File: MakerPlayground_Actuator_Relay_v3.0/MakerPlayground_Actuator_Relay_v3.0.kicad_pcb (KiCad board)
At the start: 2 copper layers, 45.5 x 19.9 mm, 8 parts, among them J1 Conn_01x04, J2 Terminal Block, J3 Terminal Block, K1 SANYOU_SRD_Form_C, Q1 Q_NPN_BEC

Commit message: Under editing mounting hole.
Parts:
- added REF**: MountingHole_3mm, MountingHole:MountingHole_3mm, F.Cu at (128.5, 112.5)
- added REF**: MountingHole_3mm, MountingHole:MountingHole_3mm, F.Cu at (128.5, 87.5)
- added REF**: MountingHole_3mm, MountingHole:MountingHole_3mm, F.Cu at (158.5, 112.5)
- added REF**: MountingHole_3mm, MountingHole:MountingHole_3mm, F.Cu at (158.5, 87.5)
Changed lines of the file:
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@@
-(kicad_pcb (version 20171130) (host pcbnew "(5.0.0-rc2-178-g3c7b91b96)")
+(kicad_pcb (version 20171130) (host pcbnew 5.0.2-5.fc29)
   (general
     (thickness 1.6)
-    (drawings 308)
+    (drawings 313)
     (tracks 21)
     (zones 0)
-    (modules 8)
+    (modules 12)
     (nets 9)
   )
   (page A4)
   (layers
-    (0 F.Cu signal)
-    (31 B.Cu signal)
+    (0 F.Cu signal hide)
+    (31 B.Cu signal hide)
     (32 B.Adhes user)
     (33 F.Adhes user)
@@
     (46 B.CrtYd user)
     (47 F.CrtYd user)
-    (48 B.Fab user)
-    (49 F.Fab user)
+    (48 B.Fab user hide)
+    (49 F.Fab user hide)
   )
   (setup
@@
     (pad_drill 0.762)
     (pad_to_mask_clearance 0.2)
+    (solder_mask_min_width 0.25)
     (aux_axis_origin 0 0)
     (visible_elements 7FFFFFFF)
@@
       (drillshape 0)
       (scaleselection 1)
-      (outputdirectory gerber/))
+      (outputdirectory "gerber/"))
   )
   (net 0 "")
@@
     (add_net SIG)
     (add_net VCC)
+  )
+  (module MountingHole:MountingHole_3mm (layer F.Cu)
+    (at 128.5 112.5 180)
+    (descr "Mounting Hole 3mm, no annular")
+    (tags "mounting hole 3mm no annular")
+    (attr virtual)
+    (fp_text reference REF** (at 0 -4 180) (layer F.SilkS) hide
+      (effects (font (size 1 1) (thickness 0.15)))
+    )
+    (fp_text value MountingHole_3mm (at 0 4 180) (layer F.Fab)
+      (effects (font (size 1 1) (thickness 0.15)))
+    )
+    (fp_circle (center 0 0) (end 3.25 0) (layer F.CrtYd) (width 0.05))
+    (fp_circle (center 0 0) (end 3 0) (layer Cmts.User) (width 0.15))
+    (fp_text user %R (at 0.3 0 180) (layer F.Fab)
+      (effects (font (size 1 1) (thickness 0.15)))
+    )
+    (pad 1 np_thru_hole circle (at 0 0 180) (size 3 3) (drill 3) (layers *.Cu *.Mask))
+  )
+  (module MountingHole:MountingHole_3mm (layer F.Cu)
+    (at 128.5 87.5 180)
+    (descr "Mounting Hole 3mm, no annular")
+    (tags "mounting hole 3mm no annular")
+    (attr virtual)
+    (fp_text reference REF** (at 0 -4 180) (layer F.SilkS) hide
+      (effects (font (size 1 1) (thickness 0.15)))
+    )
+    (fp_text value MountingHole_3mm (at 0 4 180) (layer F.Fab)
+      (effects (font (size 1 1) (thickness 0.15)))
+    )
+    (fp_text user %R (at 0.3 0 180) (layer F.Fab)
+      (effects (font (size 1 1) (thickness 0.15)))
+    )
+    (fp_circle (center 0 0) (end 3 0) (layer Cmts.User) (width 0.15))
+    (fp_circle (center 0 0) (end 3.25 0) (layer F.CrtYd) (width 0.05))
+    (pad 1 np_thru_hole circle (at 0 0 180) (size 3 3) (drill 3) (layers *.Cu *.Mask))
+  )
+  (module MountingHole:MountingHole_3mm (layer F.Cu)
+    (at 158.5 112.5)
+    (descr "Mounting Hole 3mm, no annular")
+    (tags "mounting hole 3mm no annular")
+    (attr virtual)
+    (fp_text reference REF** (at 0 -4) (layer F.SilkS) hide
+      (effects (font (size 1 1) (thickness 0.15)))
+    )
+    (fp_text value MountingHole_3mm (at 0 4) (layer F.Fab)
+      (effects (font (size 1 1) (thickness 0.15)))
+    )
+    (fp_circle (center 0 0) (end 3.25 0) (layer F.CrtYd) (width 0.05))
+    (fp_circle (center 0 0) (end 3 0) (layer Cmts.User) (width 0.15))
+    (fp_text user %R (at 0.3 0) (layer F.Fab)
+      (effects (font (size 1 1) (thickness 0.15)))
+    )
+    (pad 1 np_thru_hole circle (at 0 0) (size 3 3) (drill 3) (layers *.Cu *.Mask))
+  )
+  (module MountingHole:MountingHole_3mm (layer F.Cu)
+    (at 158.5 87.5)
+    (descr "Mounting Hole 3mm, no annular")
+    (tags "mounting hole 3mm no annular")
+    (attr virtual)
+    (fp_text reference REF** (at 0 -4) (layer F.SilkS) hide
+      (effects (font (size 1 1) (thickness 0.15)))
+    )
+    (fp_text value MountingHole_3mm (at 0 4) (layer F.Fab)
+      (effects (font (size 1 1) (thickness 0.15)))
+    )
+    (fp_text user %R (at 0.3 0) (layer F.Fab)
+      (effects (font (size 1 1) (thickness 0.15)))
+    )
+    (fp_circle (center 0 0) (end 3 0) (layer Cmts.User) (width 0.15))
+    (fp_circle (center 0 0) (end 3.25 0) (layer F.CrtYd) (width 0.05))
+    (pad 1 np_thru_hole circle (at 0 0) (size 3 3) (drill 3) (layers *.Cu *.Mask))
   )
   (module GiraffeTech-Connector:TerminalBlock_Dinkle_ED350V_1x02_P3.50mm_Horizontal (layer F.Cu)
@@
       (xy 0.199355 -0.596628) (xy 0.593328 -0.992663) (xy 0.790777 -0.991434)) (layer F.SilkS) (width 0.01))
   )
+  (dimension 25 (width 0.3) (layer Dwgs.User)
+    (gr_text "25.000 mm" (at 119.9 100 90) (layer Dwgs.User)
+      (effects (font (size 1.5 1.5) (thickness 0.3)))
+    )
+    (feature1 (pts (xy 128.5 87.5) (xy 121.413579 87.5)))
+    (feature2 (pts (xy 128.5 112.5) (xy 121.413579 112.5)))
+    (crossbar (pts (xy 122 112.5) (xy 122 87.5)))
+    (arrow1a (pts (xy 122 87.5) (xy 122.586421 88.626504)))
+    (arrow1b (pts (xy 122 87.5) (xy 121.413579 88.626504)))
+    (arrow2a (pts (xy 122 112.5) (xy 122.586421 111.373496)))
+    (arrow2b (pts (xy 122 112.5) (xy 121.413579 111.373496)))
+  )
+  (dimension 25 (width 0.3) (layer Dwgs.User)
+    (gr_text "25.000 mm" (at 167.1 100 270) (layer Dwgs.User)
+      (effects (font (size 1.5 1.5) (thickness 0.3)))
+    )
+    (feature1 (pts (xy 158.5 112.5) (xy 165.586421 112.5)))
+    (feature2 (pts (xy 158.5 87.5) (xy 165.586421 87.5)))
+    (crossbar (pts (xy 165 87.5) (xy 165 112.5)))
+    (arrow1a (pts (xy 165 112.5) (xy 164.413579 111.373496)))
+    (arrow1b (pts (xy 165 112.5) (xy 165.586421 111.373496)))
+    (arrow2a (pts (xy 165 87.5) (xy 164.413579 88.626504)))
+    (arrow2b (pts (xy 165 87.5) (xy 165.586421 88.626504)))
+  )
+  (dimension 30 (width 0.3) (layer Dwgs.User)
+    (gr_text "30.000 mm" (at 143.5 79.447319) (layer Dwgs.User)
+      (effects (font (size 1.5 1.5) (thickness 0.3)))
+    )
+    (feature1 (pts (xy 158.5 86.797319) (xy 158.5 80.960898)))
+    (feature2 (pts (xy 128.5 86.797319) (xy 128.5 80.960898)))
+    (crossbar (pts (xy 128.5 81.547319) (xy 158.5 81.547319)))
+    (arrow1a (pts (xy 158.5 81.547319) (xy 157.373496 82.13374)))
+    (arrow1b (pts (xy 158.5 81.547319) (xy 157.373496 80.960898)))
+    (arrow2a (pts (xy 128.5 81.547319) (xy 129.626504 82.13374)))
+    (arrow2b (pts (xy 128.5 81.547319) (xy 129.626504 80.960898)))
+  )
+  (gr_line (start 158.5 79) (end 158.5 114.5) (layer Dwgs.User) (width 0.2))
+  (gr_line (start 128.5 81) (end 128.5 114.25) (layer Dwgs.User) (width 0.2))
   (gr_text OUT (at 159 108.5) (layer F.SilkS)
     (effects (font (size 1.5 1.5) (thickness 0.3)))

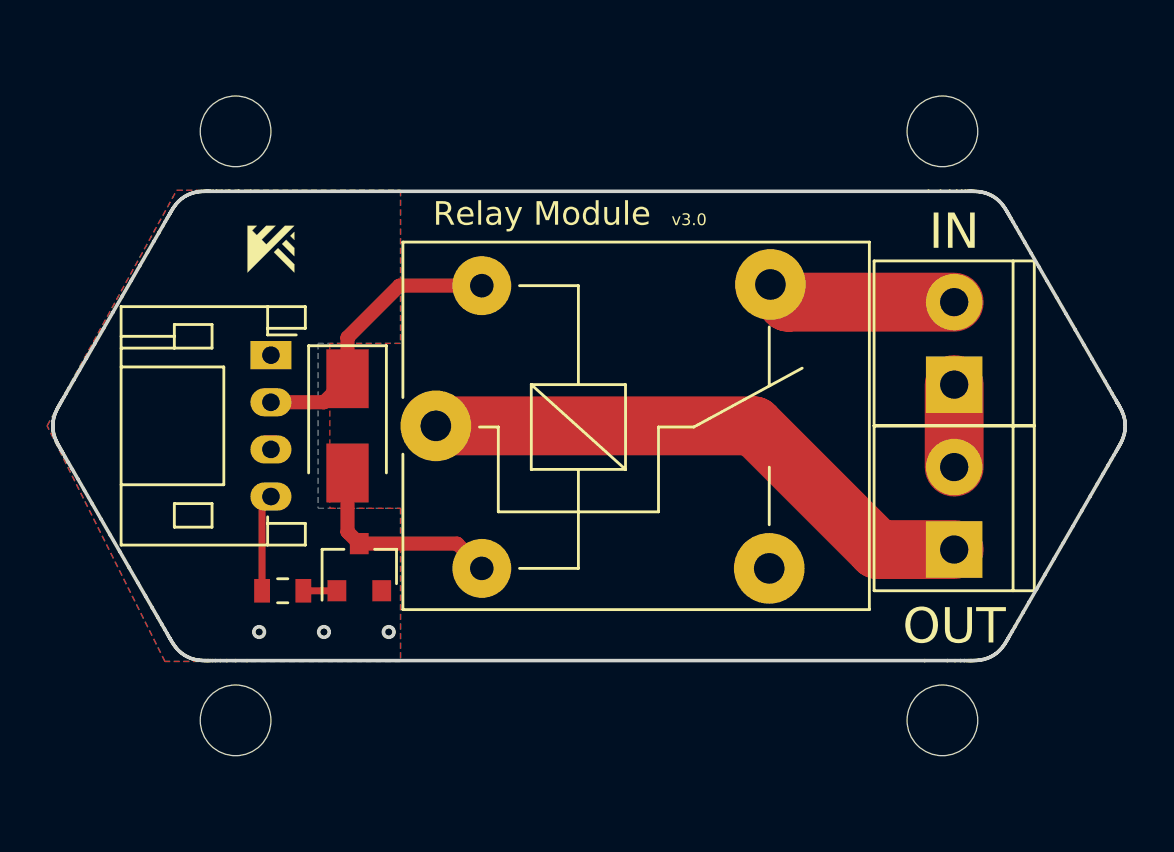
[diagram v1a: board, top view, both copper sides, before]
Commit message: Update Relay board mounting hole design.
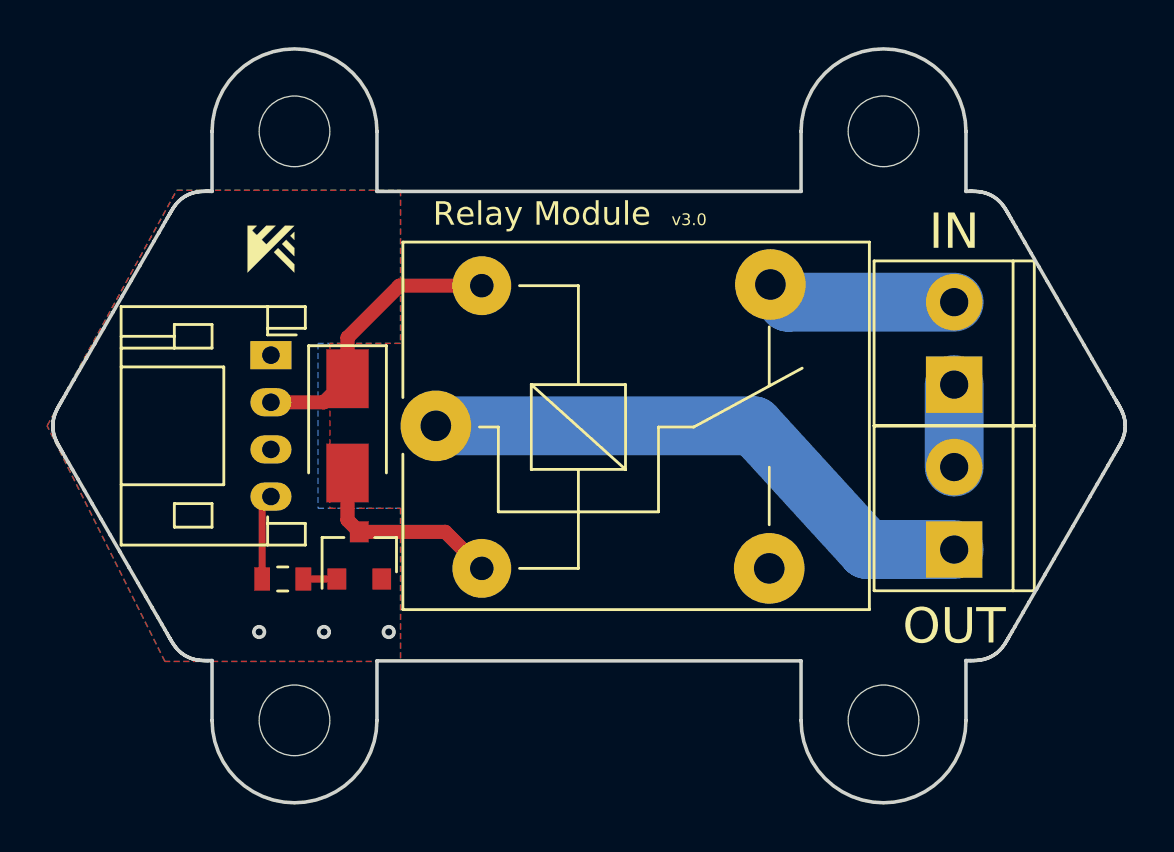
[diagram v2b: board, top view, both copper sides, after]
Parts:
- moved REF** 2.50 mm to (131.0, 112.5)
- moved REF** 2.50 mm to (131.0, 87.5)
- moved REF** 2.50 mm to (156.0, 112.5)
- moved REF** 2.50 mm to (156.0, 87.5)
- moved Q1 0.50 mm to (133.8, 105.5)
- moved R1 0.50 mm to (130.5, 106.5)
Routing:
- net SIG: track 4.16 -> 3.66 mm
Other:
- board size 45.5 x 19.9 mm -> 45.5 x 32 mm

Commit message: Update Relay PCB design & verification needed.
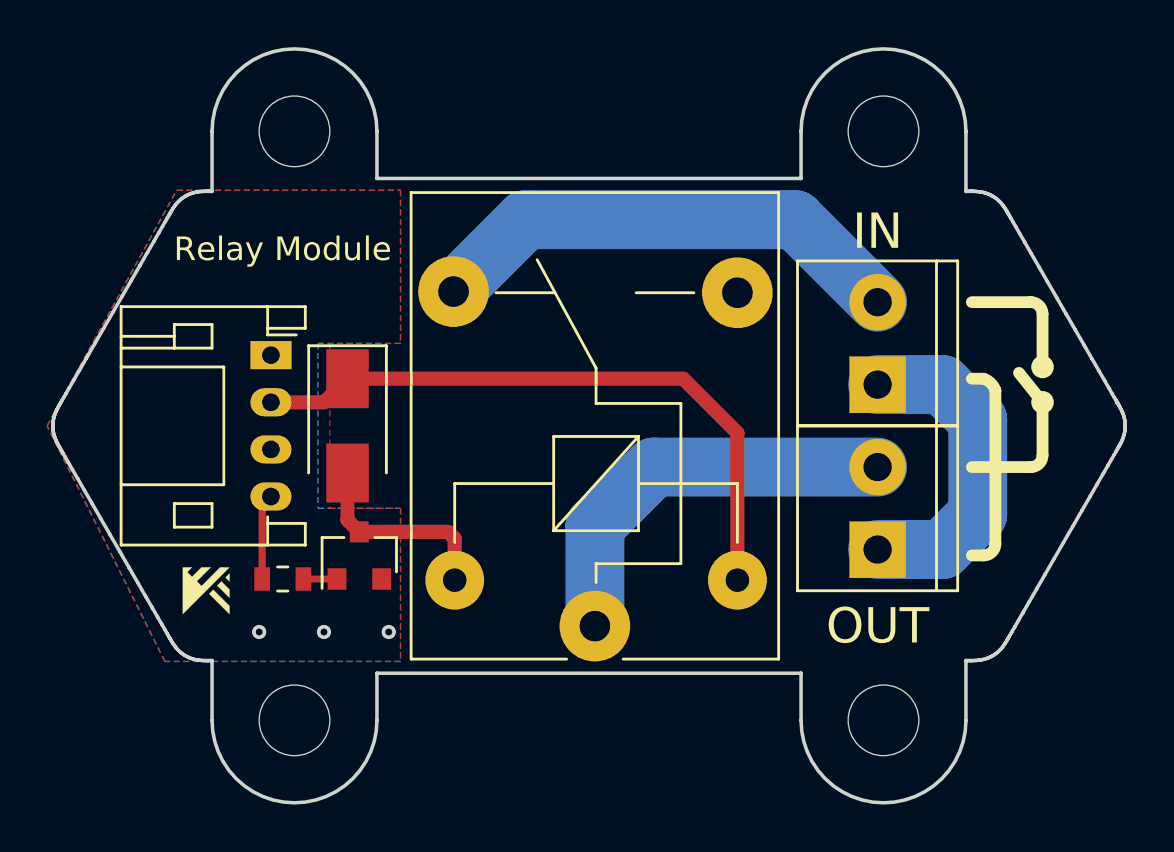
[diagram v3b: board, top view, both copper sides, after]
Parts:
- moved G*** 14.8 mm to (127.2, 107.0)
- moved K1 10.9 mm to (143.8, 108.5), turned to 90 degrees
- moved J2 3.25 mm to (155.8, 96.5)
- moved J3 3.25 mm to (155.8, 103.5)
- turned REF** to 0 degrees (x2)
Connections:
- J1 pad 3: (no net) -> Net-(J1-Pad3)
- J3 pad 1: Net-(J3-Pad1) -> Net-(J2-Pad1)
- J3 pad 2: Net-(J2-Pad1) -> Net-(J3-Pad2)
- K1 pad 1: Net-(J3-Pad1) -> Net-(J3-Pad2)
- K1 pad 2: Net-(D1-Pad2) -> VCC
- K1 pad 3: (no net) -> Net-(K1-Pad3)
- K1 pad 5: VCC -> Net-(D1-Pad2)
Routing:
- net Net-(J3-Pad1): track 24.3 -> 0.00 mm
- net Net-(J3-Pad2): track 0.00 -> 17.3 mm
- net VCC: track 12.0 -> 27.4 mm
- net Net-(J2-Pad2): track 8.11 -> 20.7 mm
- net Net-(J2-Pad1): track 3.50 -> 13.7 mm
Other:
- outline, holes or cut-outs redrawn
- board text removed: "v3.0"
